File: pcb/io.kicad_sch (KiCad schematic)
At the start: 28 parts, among them J104 USB_C_Receptacle_USB2.0_14P, J105 WORD_CLK_1, J106 WORD_CLK_2, J107 WORD_CLK_3, J108 WORD_CLK_4, J109 FPGA_JTAG, J110 STDC14_SWD, U103 74LVC2G17, U104 74LVC2G17, U105 74LVC2G17, U106 74LVC2G17

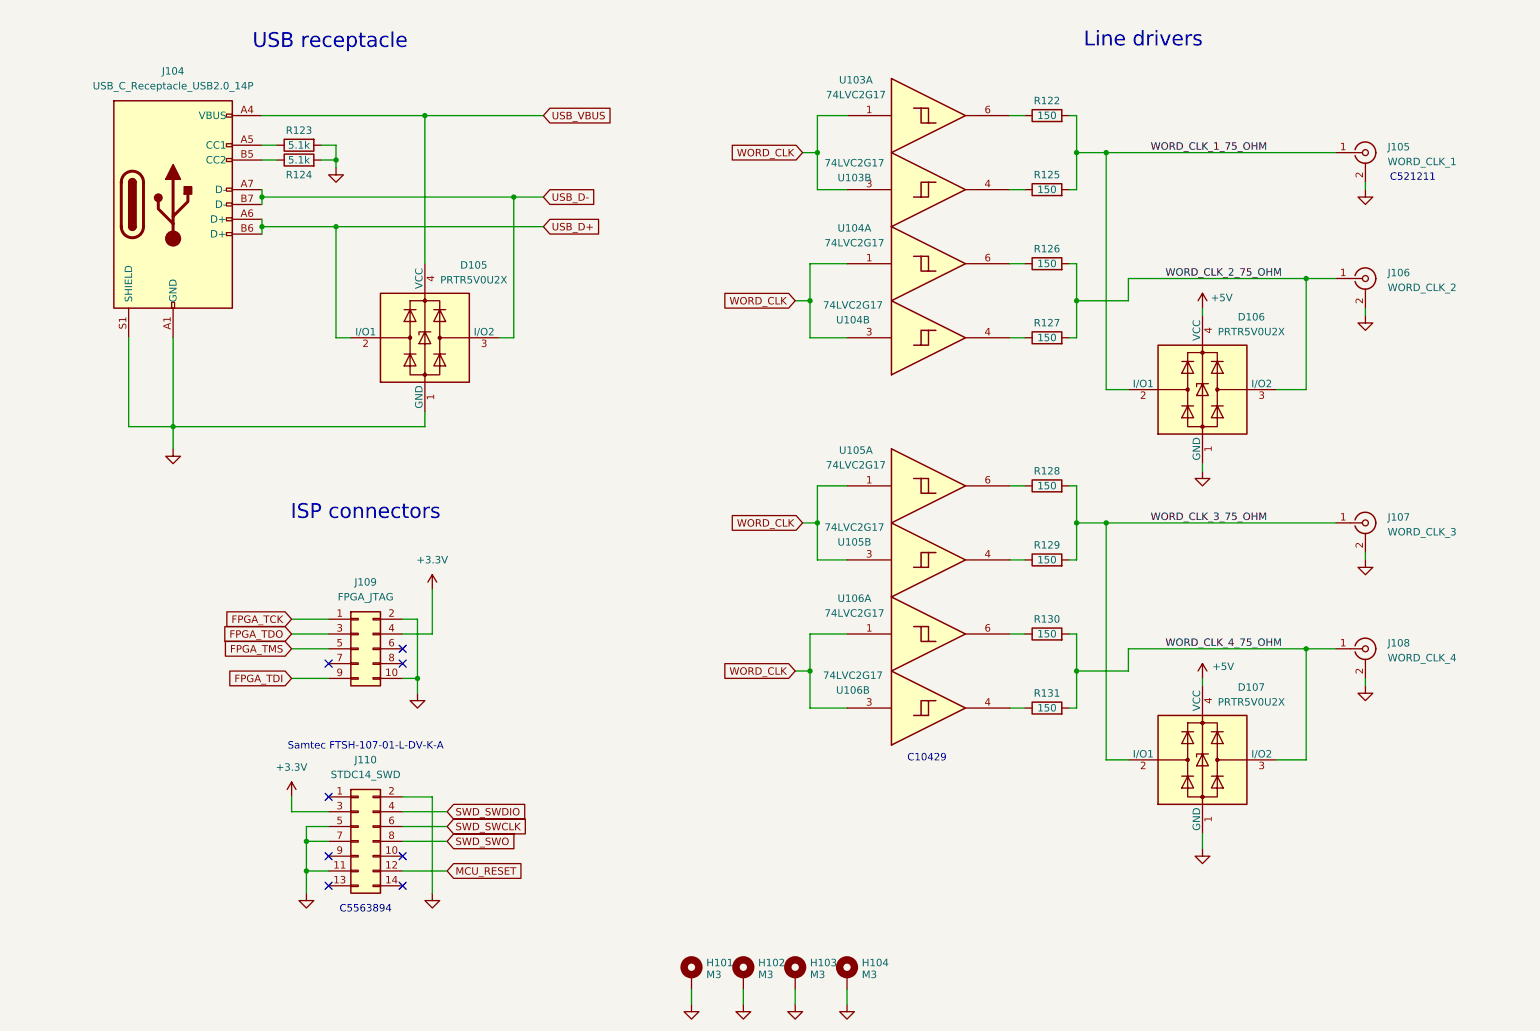
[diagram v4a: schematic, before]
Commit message: Finish drawing IO/Supply board
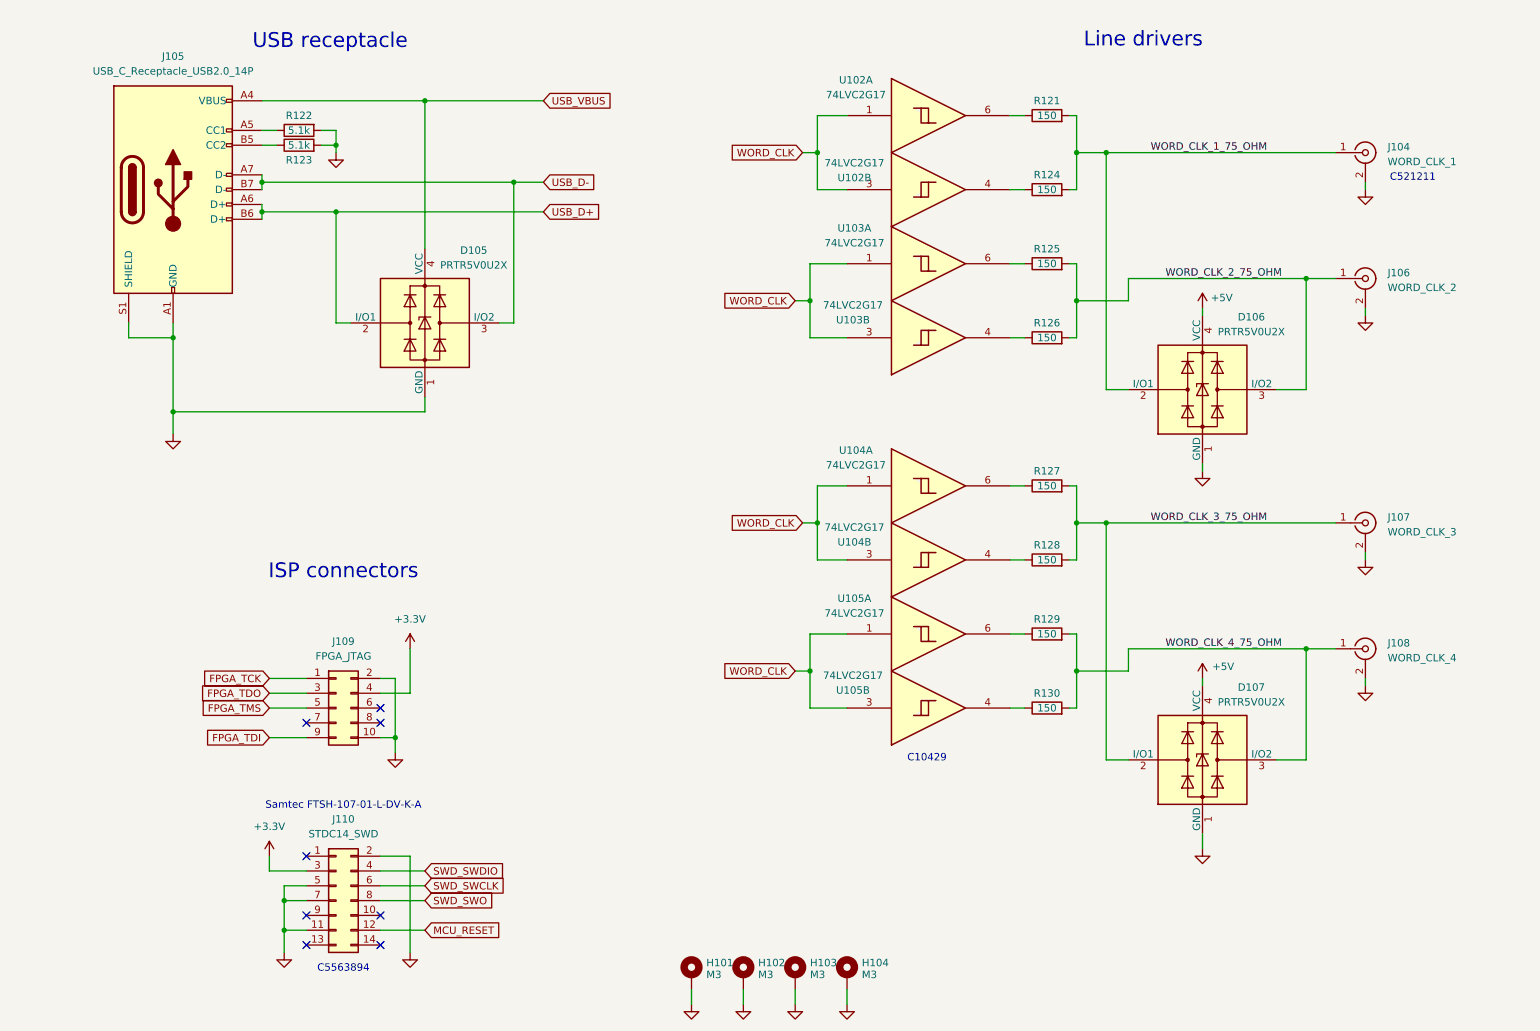
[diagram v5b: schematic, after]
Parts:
- J108: footprint Connector_IDC:IDC-Header_2x05_P2.54mm_Vertical -> adatv2:BNC_dosinconn_DOSIN-801-0051
- J109: footprint adatv2:BNC_dosinconn_DOSIN-801-0051 -> Connector_IDC:IDC-Header_2x05_P2.54mm_Vertical
- renumbered J105 to J104, J104 to J105, R122 to R121, R123 to R122, R124 to R123, R125 to R124, R126 to R125, R127 to R126, R128 to R127, R129 to R128, R130 to R129, R131 to R130, U103 to U102, U104 to U103, U105 to U104, U106 to U105
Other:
- moved on the sheet: D105, J105, J109, J110, R122, R123

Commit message: Add buffers for ADAT transfer
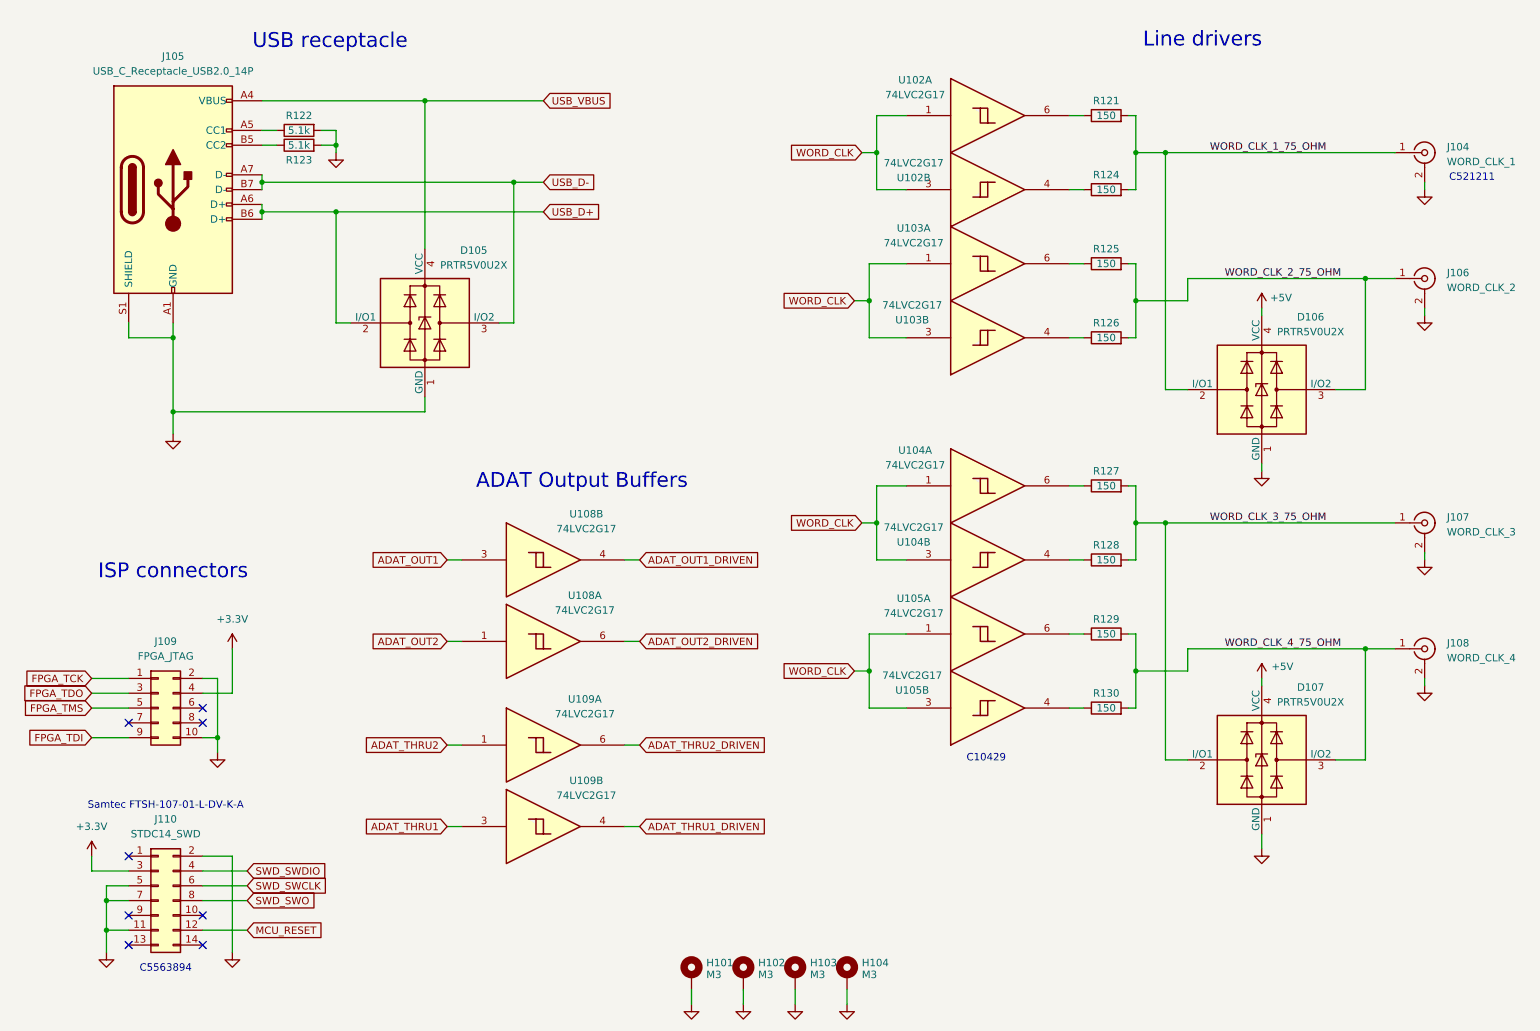
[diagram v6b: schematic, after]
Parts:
- added U108, U109: 74LVC2G17, Package_TO_SOT_SMD:SOT-23-6_Handsoldering, symbol 74xGxx:74LVC2G17
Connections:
- new net ADAT_OUT1: U108.3
- new net ADAT_OUT1_DRIVEN: U108.4
- new net ADAT_OUT2: U108.1
- new net ADAT_OUT2_DRIVEN: U108.6
- new net ADAT_THRU1: U109.3
- new net ADAT_THRU1_DRIVEN: U109.4
- new net ADAT_THRU2: U109.1
- new net ADAT_THRU2_DRIVEN: U109.6
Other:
- note added: "ADAT Output Buffers"
- moved on the sheet: D106, D107, J104, J106, J107, J108, J109, J110, R121, R124, R125, R126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

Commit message: Assign FPGA pins, change MCU to STM32F429VET6
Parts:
- R121, R124, R125, R126, R127, R128, R129, R130: value 150 -> 20
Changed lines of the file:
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@@
 			)
 		)
-		(property "Value" "150"
+		(property "Value" "20"
 			(at 205.74 110.49 90)
 			(effects
@@
 			)
 		)
-		(property "Value" "150"
+		(property "Value" "20"
 			(at 205.74 34.29 90)
 			(effects
@@
 			)
 		)
-		(property "Value" "150"
+		(property "Value" "20"
 			(at 205.74 46.99 90)
 			(effects
@@
 			)
 		)
-		(property "Value" "150"
+		(property "Value" "20"
 			(at 205.74 72.39 90)
 			(effects
@@
 			)
 		)
-		(property "Value" "150"
+		(property "Value" "20"
 			(at 205.74 135.89 90)
 			(effects
@@
 			)
 		)
-		(property "Value" "150"
+		(property "Value" "20"
 			(at 205.74 59.69 90)
 			(effects
@@
 			)
 		)
-		(property "Value" "150"
+		(property "Value" "20"
 			(at 205.74 97.79 90)
 			(effects
@@
 			)
 		)
-		(property "Value" "150"
+		(property "Value" "20"
 			(at 205.74 123.19 90)
 			(effects
